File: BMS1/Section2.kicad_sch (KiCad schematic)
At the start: 63 parts

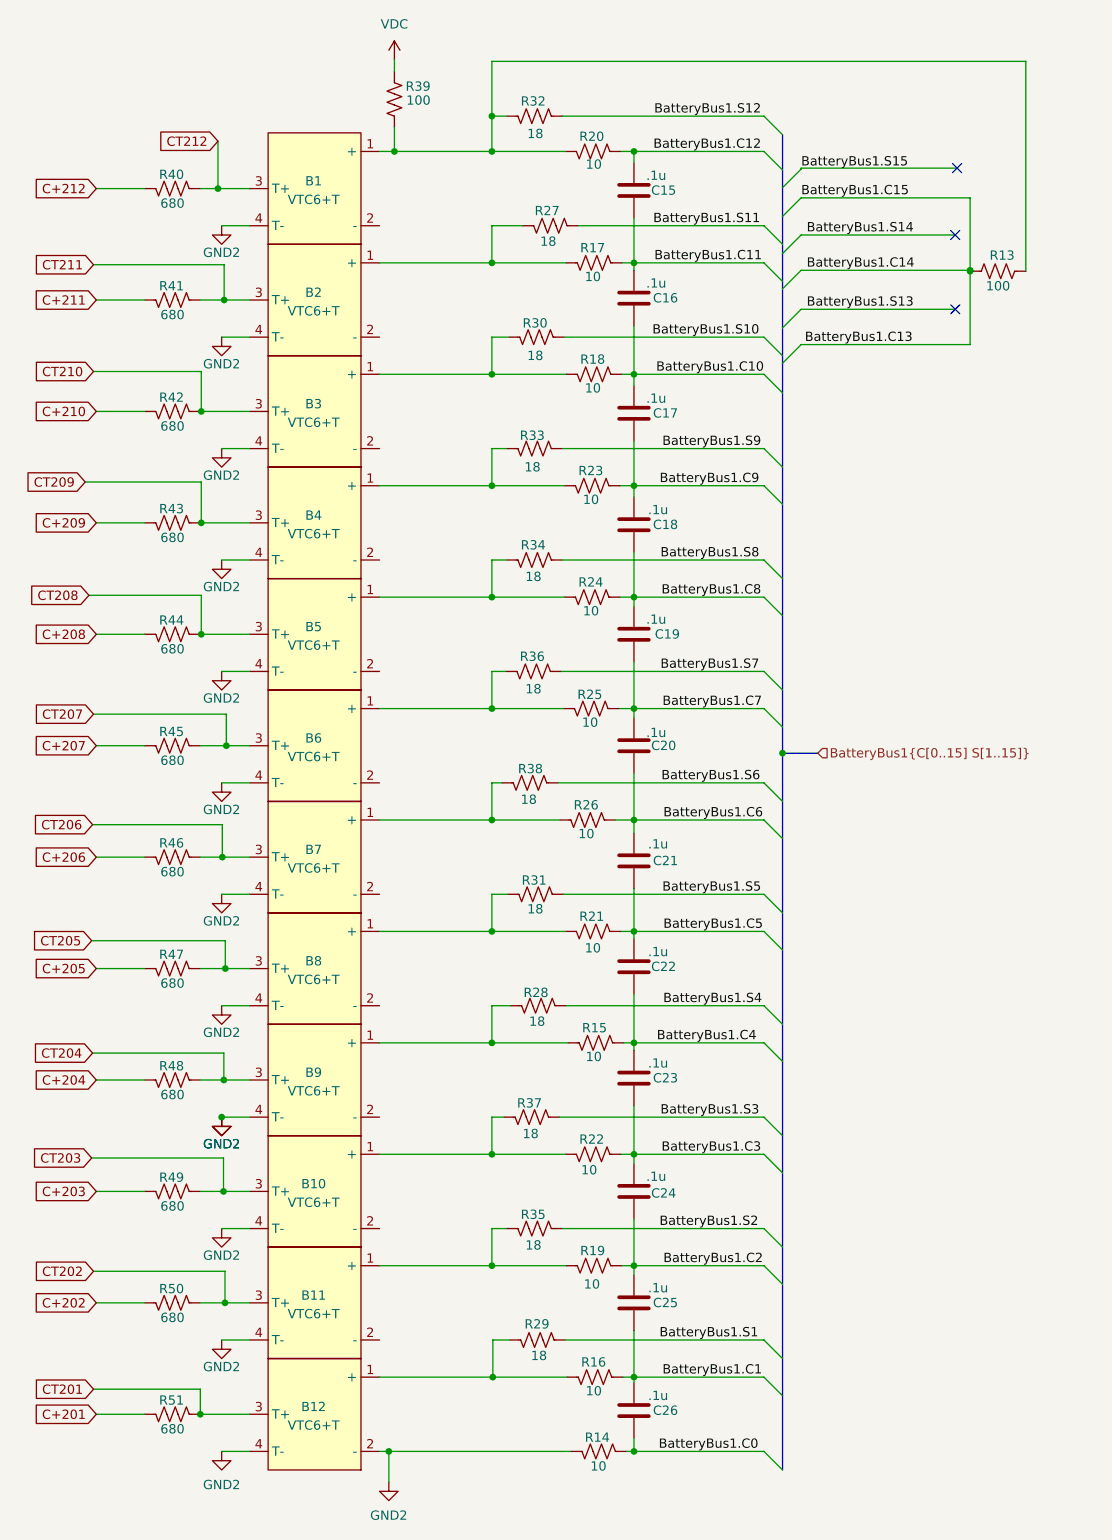
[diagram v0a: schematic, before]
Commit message: ERC fixes
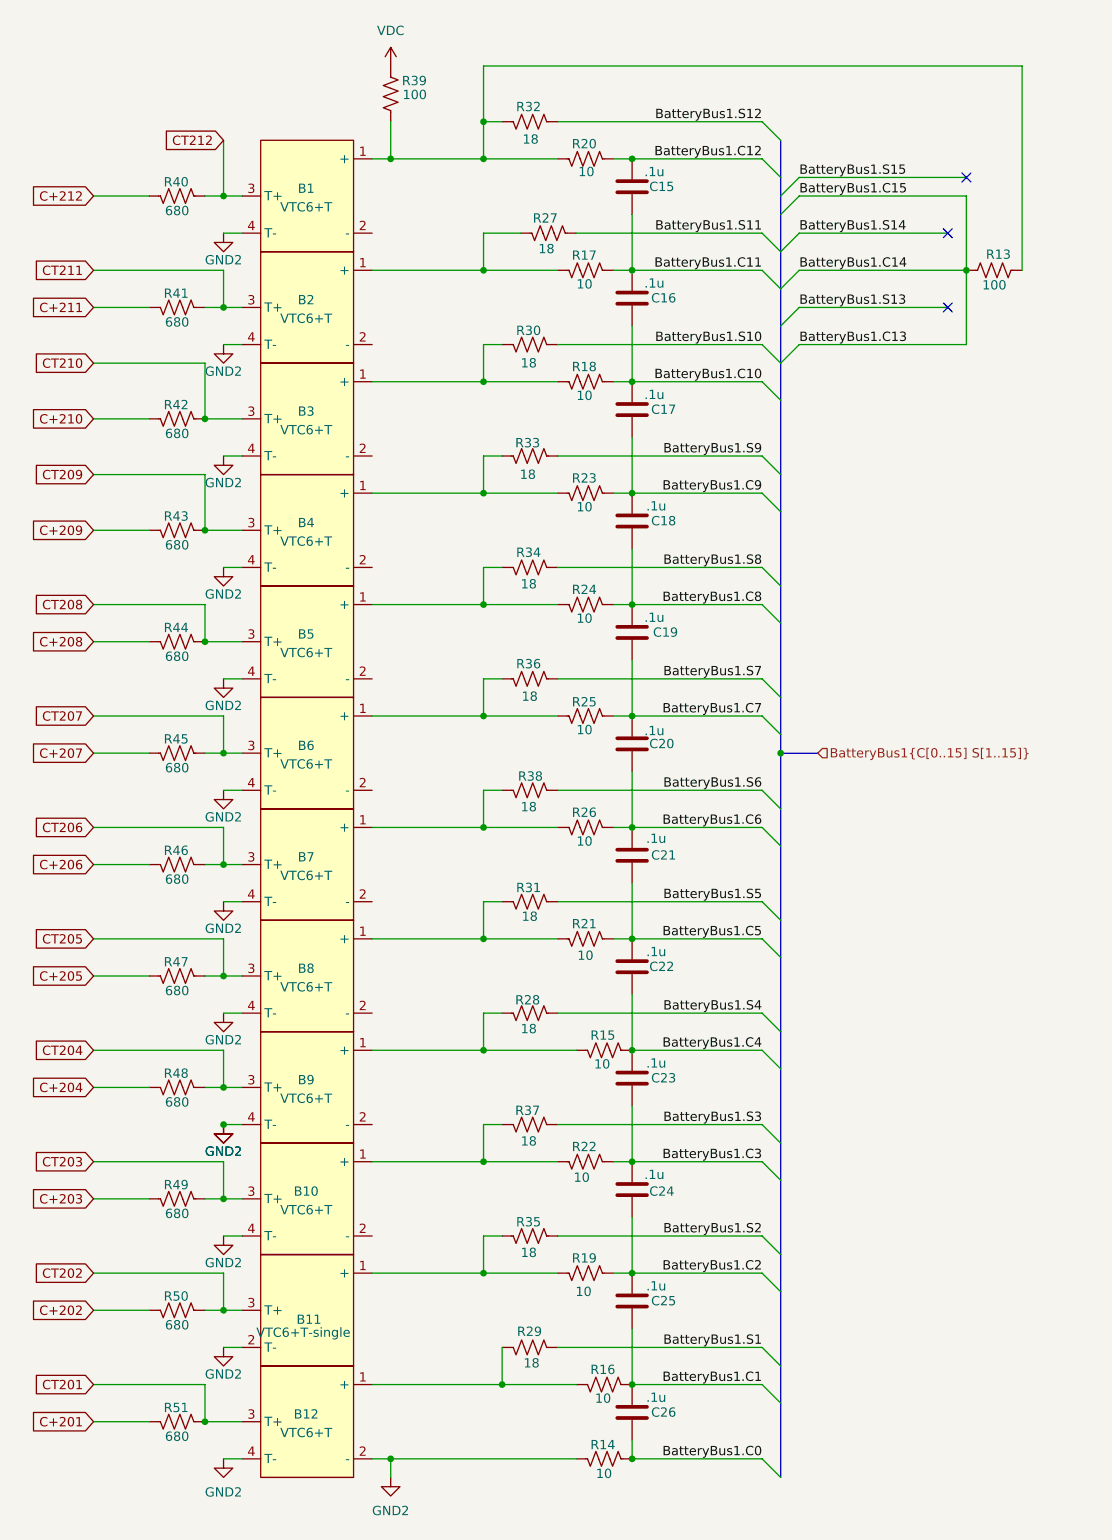
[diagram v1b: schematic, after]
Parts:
- removed B11: VTC6+T, AERO_Footprints:VTC-6, symbol AERO_Symbols:VTC6+T
- added B11: VTC6+T-single, AERO_Footprints:VTC-6-single, symbol AERO:VTC6+T-single
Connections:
- net CT202: now also B11.3 (T+)
- net GND2: now also B11.2 (T-)
- net at R19.1, R35.1: now also B11.1 (+)
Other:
- moved on the sheet: B1, B10, B12, B2, B3, B4, B5, B6, B7, B8, B9, C15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

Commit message: ERC error fixes
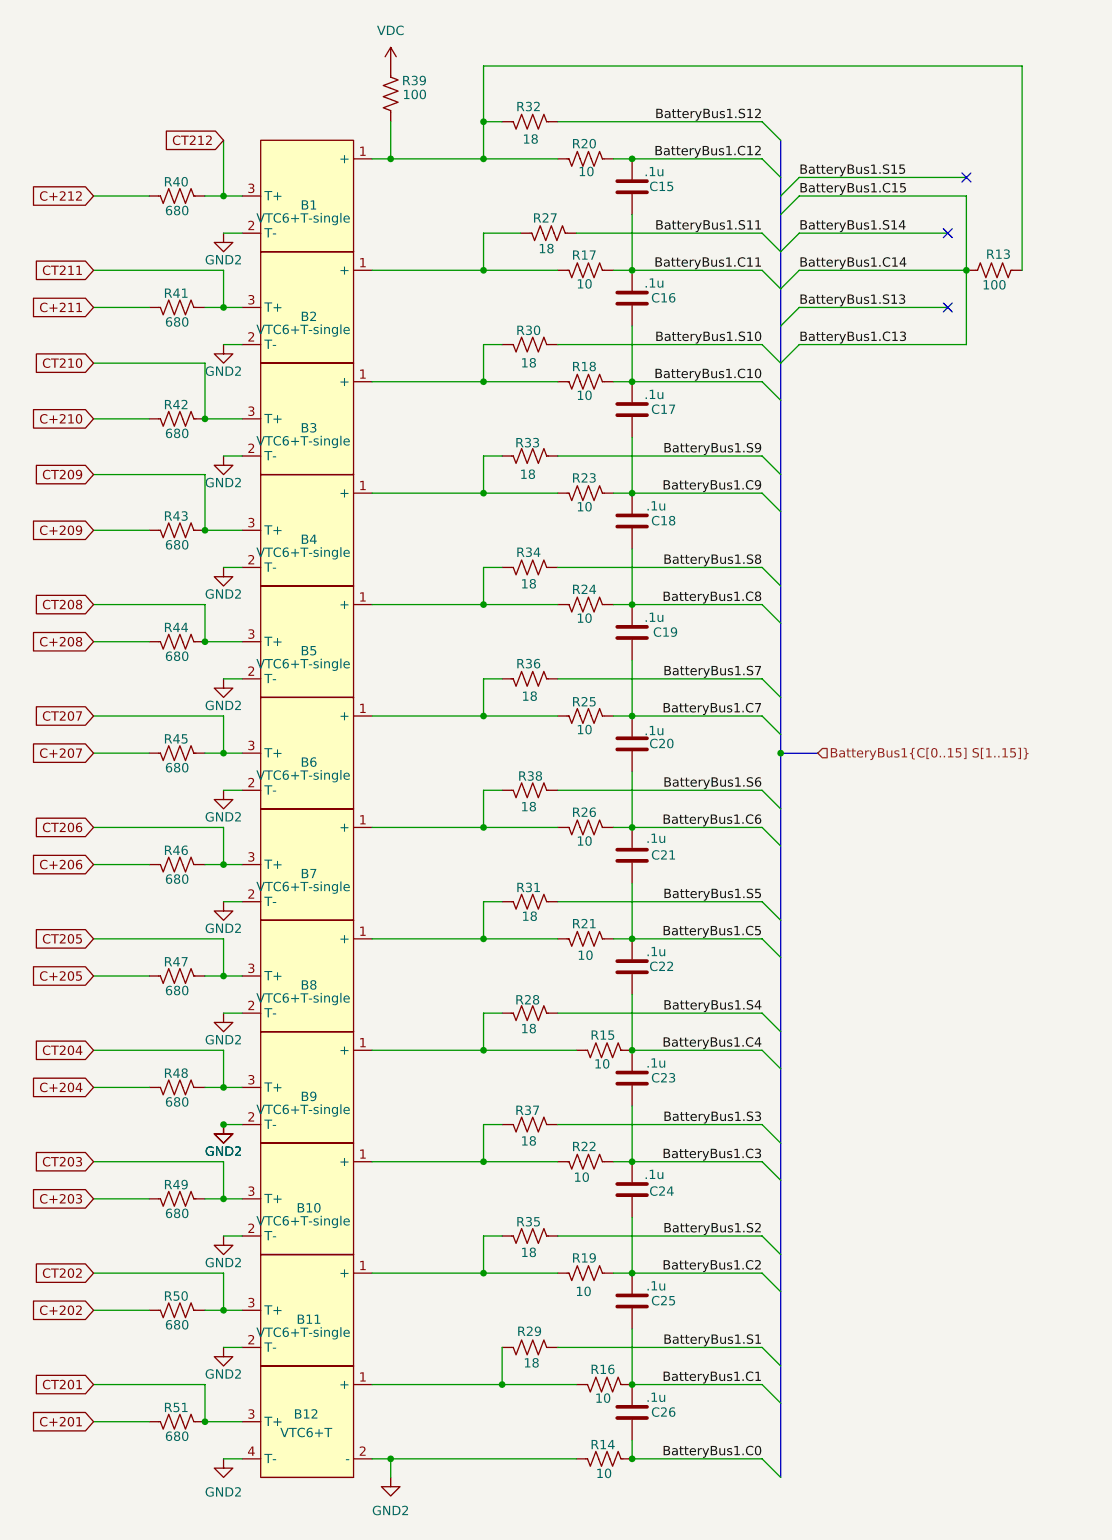
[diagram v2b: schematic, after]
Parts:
- removed B1, B10, B2, B3, B4, B5, B6, B7, B8, B9: VTC6+T, AERO_Footprints:VTC-6, symbol AERO_Symbols:VTC6+T
- added B1, B10, B2, B3, B4, B5, B6, B7, B8, B9: VTC6+T-single, AERO_Footprints:VTC-6-single, symbol AERO:VTC6+T-single
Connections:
- net CT203: now also B10.3 (T+)
- net CT204: now also B9.3 (T+)
- net CT205: now also B8.3 (T+)
- net CT206: now also B7.3 (T+)
- net CT207: now also B6.3 (T+)
- net CT208: now also B5.3 (T+)
- net CT209: now also B4.3 (T+)
- net CT210: now also B3.3 (T+)
- net CT211: now also B2.3 (T+)
- net CT212: now also B1.3 (T+)
- net GND2: now also B1.2 (T-), B10.2 (T-), B2.2 (T-), B3.2 (T-), B4.2 (T-), B5.2 (T-), B6.2 (T-), B7.2 (T-), B8.2 (T-), B9.2 (T-)
- net at R18.1, R30.1: now also B3.1 (+)
- net at R24.1, R34.1: now also B5.1 (+)
- net at R13.2, R20.1, R32.1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: now also B1.1 (+)
- net at R23.1, R33.1: now also B4.1 (+)
- net at R17.1, R27.1: now also B2.1 (+)
- net at R21.1, R31.1: now also B8.1 (+)
- net at R15.1, R28.1: now also B9.1 (+)
- net at R26.1, R38.1: now also B7.1 (+)
- net at R25.1, R36.1: now also B6.1 (+)
- net at R22.1, R37.1: now also B10.1 (+)

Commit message: Footprints
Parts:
- C15, C16, C17, C18, C19, C20, C21, C22, C23, C24, C25, C26: value .1u -> 0.1uF; footprint Capacitor_SMD:C_0603_1608Metric_Pad1.08x0.95mm_HandSolder -> Capacitor_SMD:C_0603_1608Metric; MPN (none) -> AGC0603X7R101-104KXP
- R13, R14, R15, R16, R17, R18, R19, R20, R21, R22, R23, R24, R25, R26: footprint Resistor_SMD:R_0805_2012Metric_Pad1.20x1.40mm_HandSolder -> Resistor_SMD:R_0805_2012Metric
- R27, R28, R29, R30, R31, R32, R33, R34, R35, R36, R37, R38: footprint Resistor_SMD:R_2512_6332Metric_Pad1.40x3.35mm_HandSolder -> Resistor_SMD:R_2512_6332Metric
- R39, R40, R41, R42, R43, R44, R45, R46, R47, R48, R49, R50, R51: footprint Resistor_SMD:R_0603_1608Metric_Pad0.98x0.95mm_HandSolder -> Resistor_SMD:R_0603_1608Metric

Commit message: Footprints
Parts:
- R13: MPN (none) -> RMCF0805FT100R
- R14, R15, R16, R17, R18, R19, R20, R21, R22, R23, R24, R25, R26: MPN (none) -> ERJ-P06J100V
- R39: MPN (none) -> ERJ-3EKF1000V
- R40, R41, R42, R43, R44, R45, R46, R47, R48, R49, R50, R51: MPN (none) -> RC0603JR-07680RL
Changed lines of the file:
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@@
 			)
 		)
-		(property "Datasheet" "~"
+		(property "Datasheet" "https://www.yageo.com/upload/media/product/products/datasheet/rchip/PYu-RC_Group_51_RoHS_L_12.pdf"
 			(at 52.07 78.74 0)
 			(effects
@@
 			)
 		)
-		(property "MPN" ""
+		(property "MPN" "RC0603JR-07680RL"
 			(at 52.07 78.74 0)
 			(effects
@@
 			)
 		)
-		(property "Datasheet" "~"
+		(property "Datasheet" "https://www.yageo.com/upload/media/product/products/datasheet/rchip/PYu-RC_Group_51_RoHS_L_12.pdf"
 			(at 52.07 63.5 0)
 			(effects
@@
 			)
 		)
-		(property "MPN" ""
+		(property "MPN" "RC0603JR-07680RL"
 			(at 52.07 63.5 0)
 			(effects
@@
 			)
 		)
-		(property "Datasheet" "~"
+		(property "Datasheet" "https://industrial.panasonic.com/cdbs/www-data/pdf/RDO0000/AOA0000C331.pdf"
 			(at 107.95 88.9 0)
 			(effects
@@
 			)
 		)
-		(property "MPN" ""
+		(property "MPN" "ERJ-P06J100V"
 			(at 107.95 88.9 0)
 			(effects
@@
 			)
 		)
-		(property "Datasheet" "~"
+		(property "Datasheet" "https://www.yageo.com/upload/media/product/products/datasheet/rchip/PYu-RC_Group_51_RoHS_L_12.pdf"
 			(at 52.07 109.22 0)
 			(effects
@@
 			)
 		)
-		(property "MPN" ""
+		(property "MPN" "RC0603JR-07680RL"
 			(at 52.07 109.22 0)
 			(effects
@@
 			)
 		)
-		(property "Datasheet" "~"
+		(property "Datasheet" "https://industrial.panasonic.com/cdbs/www-data/pdf/RDO0000/AOA0000C331.pdf"
 			(at 107.95 149.86 0)
 			(effects
@@
 			)
 		)
-		(property "MPN" ""
+		(property "MPN" "ERJ-P06J100V"
 			(at 107.95 149.86 0)
 			(effects
@@
 			)
 		)
-		(property "Datasheet" "~"
+		(property "Datasheet" "https://industrial.panasonic.com/cdbs/www-data/pdf/RDA0000/AOA0000C304.pdf"
 			(at 81.28 34.29 0)
 			(effects
@@
 			)
 		)
-		(property "MPN" ""
+		(property "MPN" "ERJ-3EKF1000V"
 			(at 81.28 34.29 0)
 			(effects
@@
 			)
 		)
-		(property "Datasheet" "~"
+		(property "Datasheet" "https://www.yageo.com/upload/media/product/products/datasheet/rchip/PYu-RC_Group_51_RoHS_L_12.pdf"
 			(at 52.07 48.26 0)
 			(effects
@@
 			)
 		)
-		(property "MPN" ""
+		(property "MPN" "RC0603JR-07680RL"
 			(at 52.07 48.26 0)
 			(effects
@@
 			)
 		)
-		(property "Datasheet" "~"
+		(property "Datasheet" "https://industrial.panasonic.com/cdbs/www-data/pdf/RDO0000/AOA0000C331.pdf"
 			(at 110.49 220.98 0)
 			(effects
@@
 			)
 		)
-		(property "MPN" ""
+		(property "MPN" "ERJ-P06J100V"
 			(at 110.49 220.98 0)
 			(effects
@@
 			)
 		)
-		(property "Datasheet" "~"
+		(property "Datasheet" "https://industrial.panasonic.com/cdbs/www-data/pdf/RDO0000/AOA0000C331.pdf"
 			(at 107.95 73.66 0)
 			(effects
@@
 			)
 		)
-		(property "MPN" ""
+		(property "MPN" "ERJ-P06J100V"
 			(at 107.95 73.66 0)
 			(effects
@@
 			)
 		)
-		(property "Datasheet" "~"
+		(property "Datasheet" "https://industrial.panasonic.com/cdbs/www-data/pdf/RDO0000/AOA0000C331.pdf"
 			(at 107.95 43.18 0)
 			(effects
@@
 			)
 		)
-		(property "MPN" ""
+		(property "MPN" "ERJ-P06J100V"
 			(at 107.95 43.18 0)
 			(effects
@@
 			)
 		)
-		(property "Datasheet" "~"
+		(property "Datasheet" "https://www.yageo.com/upload/media/product/products/datasheet/rchip/PYu-RC_Group_51_RoHS_L_12.pdf"
 			(at 52.07 139.7 0)
 			(effects
@@
 			)
 		)
-		(property "MPN" ""
+		(property "MPN" "RC0603JR-07680RL"
 			(at 52.07 139.7 0)
 			(effects
@@
 			)
 		)
-		(property "Datasheet" ""
+		(property "Datasheet" "https://www.seielect.com/catalog/sei-rmcf_rmcp.pdf"
 			(at 163.83 58.42 0)
 			(effects
@@
 			)
 		)
-		(property "MPN" ""
+		(property "MPN" "RMCF0805FT100R"
 			(at 163.83 58.42 0)
 			(effects
@@
 			)
 		)
-		(property "Datasheet" "~"
+		(property "Datasheet" "https://industrial.panasonic.com/cdbs/www-data/pdf/RDO0000/AOA0000C331.pdf"
 			(at 107.95 104.14 0)
 			(effects
@@
 			)
 		)
-		(property "MPN" ""
+		(property "MPN" "ERJ-P06J100V"
 			(at 107.95 104.14 0)
 			(effects
@@
 			)
 		)
-		(property "Datasheet" "~"
+		(property "Datasheet" "https://industrial.panasonic.com/cdbs/www-data/pdf/RDO0000/AOA0000C331.pdf"
 			(at 110.49 165.1 0)
 			(effects
@@
 			)
 		)
-		(property "MPN" ""
+		(property "MPN" "ERJ-P06J100V"
 			(at 110.49 165.1 0)
 			(effects
@@
 			)
 		)
-		(property "Datasheet" "~"
+		(property "Datasheet" "https://www.yageo.com/upload/media/product/products/datasheet/rchip/PYu-RC_Group_51_RoHS_L_12.pdf"
 			(at 52.07 185.42 0)
 			(effects
@@
 			)
 		)
-		(property "MPN" ""
+		(property "MPN" "RC0603JR-07680RL"
 			(at 52.07 185.42 0)
 			(effects
@@
 			)
 		)
-		(property "Datasheet" "~"
+		(property "Datasheet" "https://industrial.panasonic.com/cdbs/www-data/pdf/RDO0000/AOA0000C331.pdf"
 			(at 107.95 180.34 0)
 			(effects
@@
 			)
 		)
-		(property "MPN" ""
+		(property "MPN" "ERJ-P06J100V"
 			(at 107.95 180.34 0)
 			(effects
@@
 			)
 		)
-		(property "Datasheet" "~"
+		(property "Datasheet" "https://industrial.panasonic.com/cdbs/www-data/pdf/RDO0000/AOA0000C331.pdf"
 			(at 107.95 58.42 0)
 			(effects
@@
 			)
 		)
-		(property "MPN" ""
+		(property "MPN" "ERJ-P06J100V"
 			(at 107.95 58.42 0)
 			(effects
@@
 			)
 		)
-		(property "Datasheet" "~"
+		(property "Datasheet" "https://industrial.panasonic.com/cdbs/www-data/pdf/RDO0000/AOA0000C331.pdf"
 			(at 110.49 210.82 0)
 			(effects
@@
 			)
 		)
-		(property "MPN" ""
+		(property "MPN" "ERJ-P06J100V"
 			(at 110.49 210.82 0)
 			(effects
@@
 			)
 		)
-		(property "Datasheet" "~"
+		(property "Datasheet" "https://www.yageo.com/upload/media/product/products/datasheet/rchip/PYu-RC_Group_51_RoHS_L_12.pdf"
 			(at 52.07 215.9 0)
 			(effects
@@
 			)
 		)
-		(property "MPN" ""
+		(property "MPN" "RC0603JR-07680RL"
 			(at 52.07 215.9 0)
 			(effects
@@
 			)
 		)
-		(property "Datasheet" "~"
+		(property "Datasheet" "https://www.yageo.com/upload/media/product/products/datasheet/rchip/PYu-RC_Group_51_RoHS_L_12.pdf"
 			(at 52.07 200.66 0)
 			(effects
@@
 			)
 		)
-		(property "MPN" ""
+		(property "MPN" "RC0603JR-07680RL"
 			(at 52.07 200.66 0)
 			(effects
@@
 			)
 		)
-		(property "Datasheet" "~"
+		(property "Datasheet" "https://industrial.panasonic.com/cdbs/www-data/pdf/RDO0000/AOA0000C331.pdf"
 			(at 107.95 134.62 0)
 			(effects
@@
 			)
 		)
-		(property "MPN" ""
+		(property "MPN" "ERJ-P06J100V"
 			(at 107.95 134.62 0)
 			(effects
@@
 			)
 		)
-		(property "Datasheet" "~"
+		(property "Datasheet" "https://industrial.panasonic.com/cdbs/www-data/pdf/RDO0000/AOA0000C331.pdf"
 			(at 107.95 195.58 0)
 			(effects
@@
 			)
 		)
-		(property "MPN" ""
+		(property "MPN" "ERJ-P06J100V"
 			(at 107.95 195.58 0)
 			(effects
@@
 			)
 		)
-		(property "Datasheet" "~"
+		(property "Datasheet" "https://www.yageo.com/upload/media/product/products/datasheet/rchip/PYu-RC_Group_51_RoHS_L_12.pdf"
 			(at 52.07 93.98 0)
 			(effects
@@
 			)
 		)
-		(property "MPN" ""
+		(property "MPN" "RC0603JR-07680RL"
 			(at 52.07 93.98 0)
 			(effects
@@
 			)
 		)
-		(property "Datasheet" "~"
+		(property "Datasheet" "https://www.yageo.com/upload/media/product/products/datasheet/rchip/PYu-RC_Group_51_RoHS_L_12.pdf"
 			(at 52.07 170.18 0)
 			(effects
@@
 			)
 		)
-		(property "MPN" ""
+		(property "MPN" "RC0603JR-07680RL"
 			(at 52.07 170.18 0)
 			(effects
@@
 			)
 		)
-		(property "Datasheet" "~"
+		(property "Datasheet" "https://www.yageo.com/upload/media/product/products/datasheet/rchip/PYu-RC_Group_51_RoHS_L_12.pdf"
 			(at 52.07 154.94 0)
 			(effects
@@
 			)
 		)
-		(property "MPN" ""
+		(property "MPN" "RC0603JR-07680RL"
 			(at 52.07 154.94 0)
 			(effects
@@
 			)
 		)
-		(property "Datasheet" "~"
+		(property "Datasheet" "https://www.yageo.com/upload/media/product/products/datasheet/rchip/PYu-RC_Group_51_RoHS_L_12.pdf"
 			(at 52.07 124.46 0)
 			(effects
@@
 			)
 		)
-		(property "MPN" ""
+		(property "MPN" "RC0603JR-07680RL"
 			(at 52.07 124.46 0)
 			(effects
@@
 			)
 		)
-		(property "Datasheet" "~"
+		(property "Datasheet" "https://industrial.panasonic.com/cdbs/www-data/pdf/RDO0000/AOA0000C331.pdf"
 			(at 107.95 119.38 0)
 			(effects
@@
 			)
 		)
-		(property "MPN" ""
+		(property "MPN" "ERJ-P06J100V"
 			(at 107.95 119.38 0)
 			(effects
